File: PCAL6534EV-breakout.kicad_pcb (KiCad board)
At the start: 6 copper layers, 15.2 x 50.8 mm, 14 parts, among them J1 SM04B-SRSS-TB, J2 Conn_01x20, J3 Conn_01x20, J4 Conn_02x04_Odd_Even, U1 PCAL6534EV

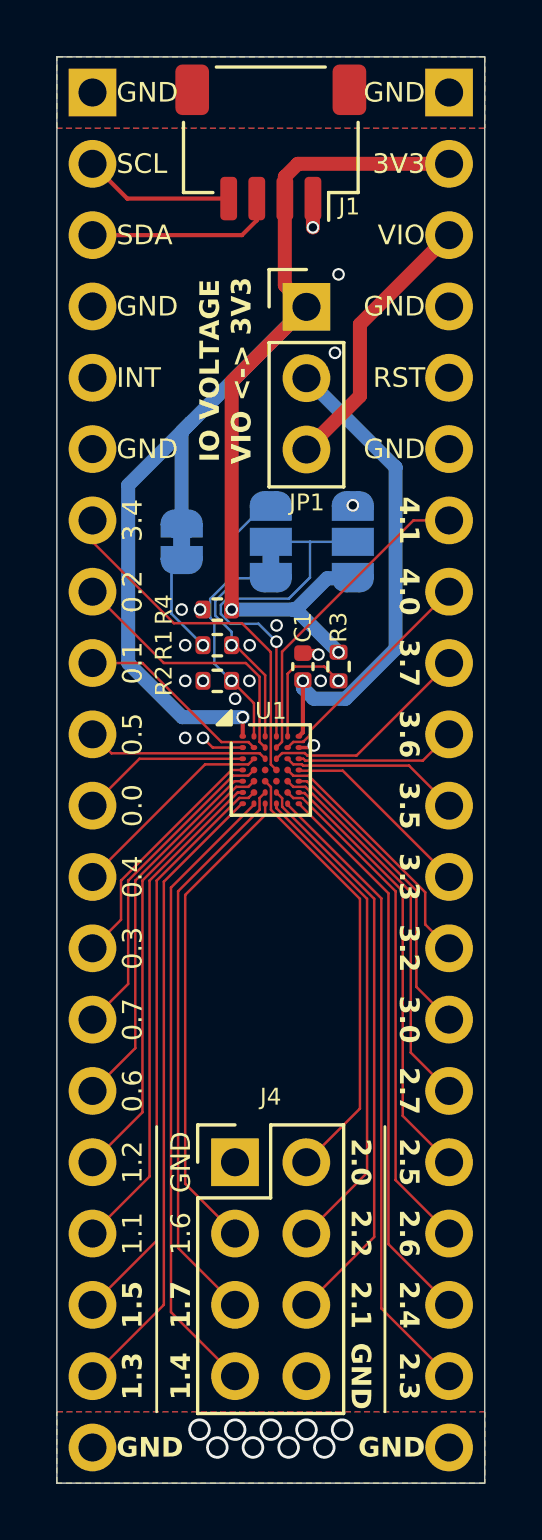
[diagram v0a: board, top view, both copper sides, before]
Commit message: add more art
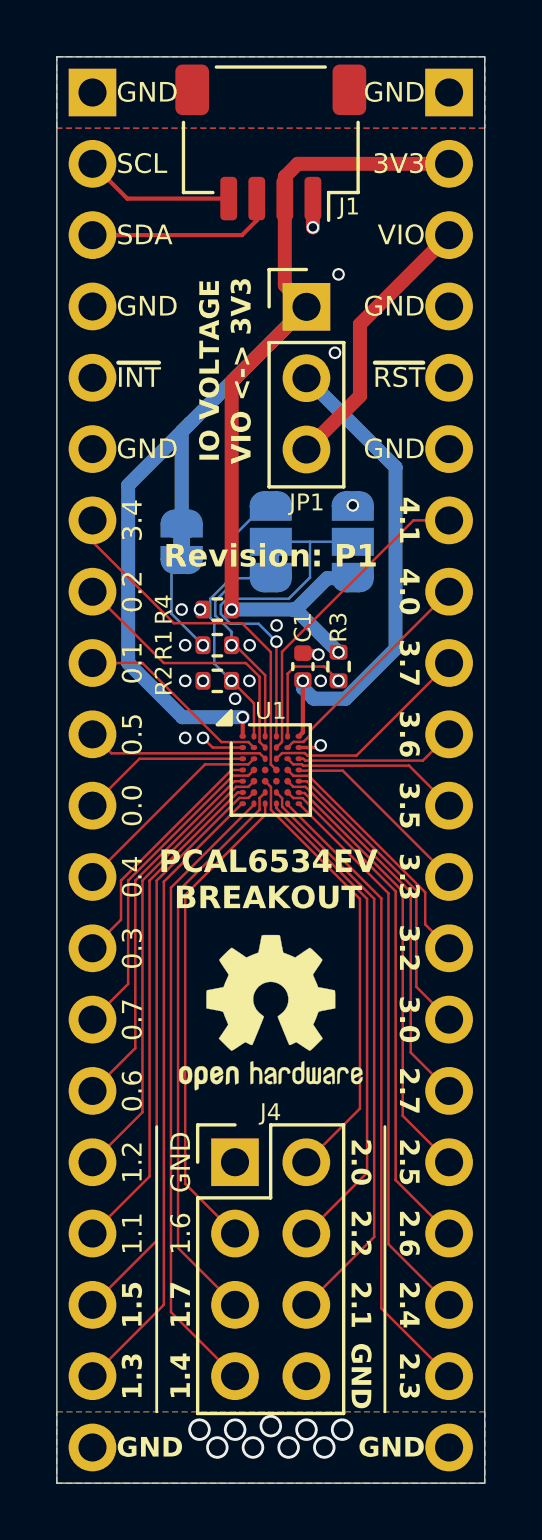
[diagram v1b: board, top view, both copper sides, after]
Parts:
- added REF**: OSHW-Logo2_7.3x6mm_SilkScreen, Symbol:OSHW-Logo2_7.3x6mm_SilkScreen, F.Cu at (155.0, 119.1)
- added REF**: KiCad-Logo2_5mm_SilkScreen, Symbol:KiCad-Logo2_5mm_SilkScreen, B.Cu at (156.3, 116.3)
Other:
- board text added: "(C) Joel Michael, 2024 License: CERN-OHL-W"
- board text added: "0b01000XY Default: 0x20"
- board text added: "I2C-DEVICE ADDRESS"
- board text added: "I2C-PULLUP DISABLE"
- board text added: "PCAL6534EV BREAKOUT"
- board text added: "Revision: P1"
- board text added: "SERIAL: P1-"
- board text added: "~{INT}"
- board text added: "~{RST}"
- board text removed: "INT"
- board text removed: "RST"
